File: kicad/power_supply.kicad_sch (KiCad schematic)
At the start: 60 parts, among them J2 Cliff DC10A, Q1 2N2905A, Q2 2N2905A, Q3 2N3904, Q4 2N3904, U11 7406, U16 MC34063AP, U18 LM7805_TO220, U19 LM317SP_TO220, U20 LM317SP_TO220

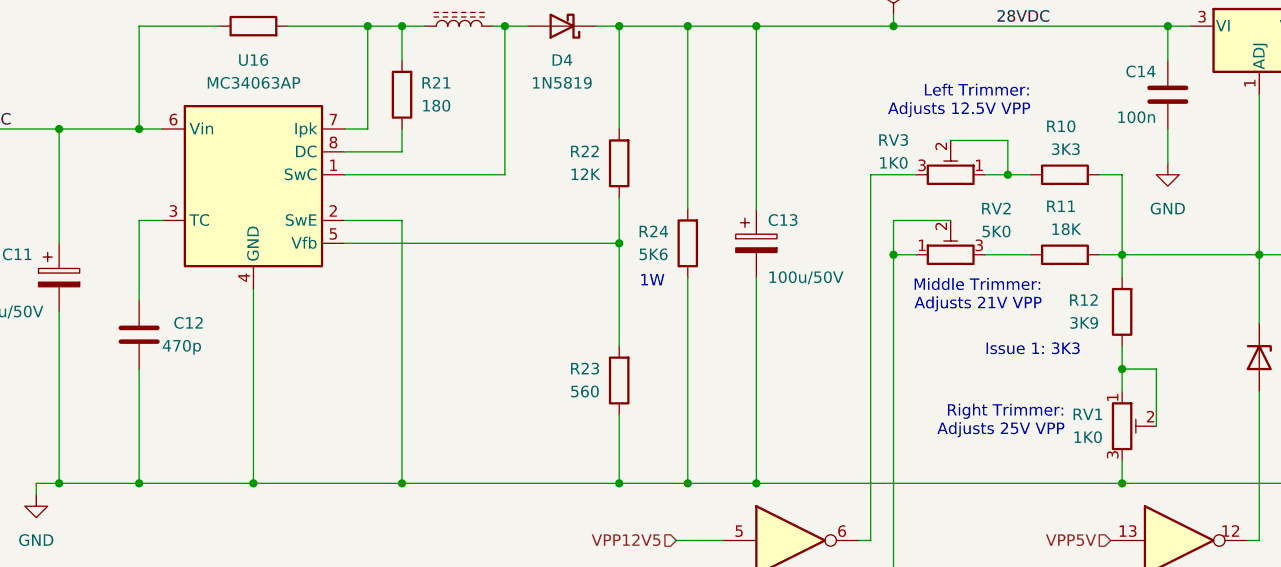
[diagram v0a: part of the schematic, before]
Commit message: KiCAD: Tweak boost convertor values
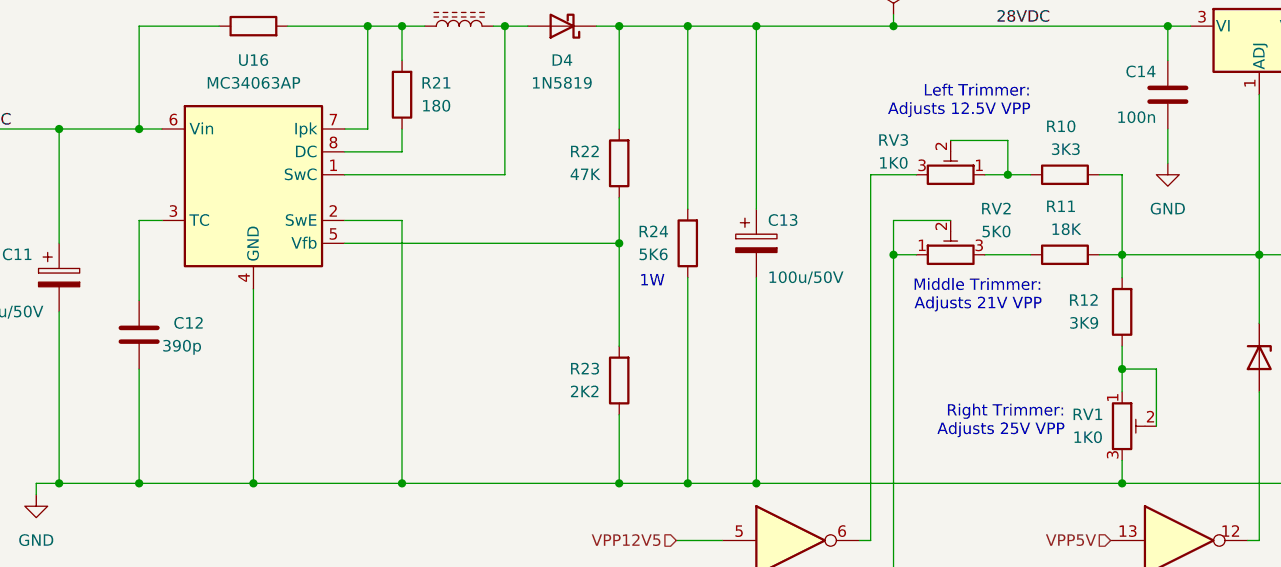
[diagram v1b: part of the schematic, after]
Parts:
- C12: value 470p -> 390p
- R22: value 12K -> 47K
- R23: value 560 -> 2K2
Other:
- note removed: "Issue 1: 3K3"
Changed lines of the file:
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@@
     (effects (font (size 1.27 1.27)) (justify right bottom))
-  )
-  (text "Issue 1: 3K3" (at 151.13 66.04 0)
-    (effects (font (size 1.27 1.27)) (justify left bottom))
   )
   (text "Indicates\nsocket is\npowered" (at 261.62 134.62 0)
@@
       (effects (font (size 1.27 1.27)) (justify right))
     )
-    (property "Value" "470p" (id 1) (at 59.69 64.77 0)
+    (property "Value" "390p" (id 1) (at 59.69 64.77 0)
       (effects (font (size 1.27 1.27)) (justify right))
     )
@@
     (in_bom yes) (on_board yes)
     (property "Reference" "R23" (id 0) (at 106.68 67.31 0))
-    (property "Value" "560" (id 1) (at 106.68 69.85 0))
+    (property "Value" "2K2" (id 1) (at 106.68 69.85 0))
     (property "Footprint" "custom_footprints:R_Axial_DIN0207_L6.3mm_D2.0mm_P10.16mm_Horizontal" (id 2) (at 112.268 68.58 90)
       (effects (font (size 1.27 1.27)) hide)
@@
     (in_bom yes) (on_board yes)
     (property "Reference" "R22" (id 0) (at 106.68 43.18 0))
-    (property "Value" "12K" (id 1) (at 106.68 45.72 0))
+    (property "Value" "47K" (id 1) (at 106.68 45.72 0))
     (property "Footprint" "custom_footprints:R_Axial_DIN0207_L6.3mm_D2.0mm_P10.16mm_Horizontal" (id 2) (at 112.268 44.45 90)
       (effects (font (size 1.27 1.27)) hide)

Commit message: KiCAD: Add heatsinks
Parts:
- added HS1: Multicomp Pro MC33263, custom_footprints:Heatsink_Fischer_SK104-STC-STIC_35x13mm_2xDrill2.5mm, symbol Mechanical:Heatsink_Pad
- added HS2, HS3: Clip On Heatsink, custom_footprints:Heatsink_Boyd_PF720, symbol Mechanical:Heatsink
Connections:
- net GND: now also HS1.1
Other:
- note removed: "Mounted on Heatsink"
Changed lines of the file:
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@@
     (effects (font (size 1.27 1.27)) (justify left bottom))
-  )
-  (text "Mounted on Heatsink" (at 68.58 124.46 180)
-    (effects (font (size 1.27 1.27)) (justify right bottom))
   )
   (text "Indicates\nboard is\npowered" (at 124.46 127 0)
@@
   (symbol (lib_id "Regulator_Linear:LM7805_TO220") (at 57.15 127 0) (unit 1)
     (in_bom yes) (on_board yes)
-    (property "Reference" "U18" (id 0) (at 57.15 118.11 0))
-    (property "Value" "LM7805_TO220" (id 1) (at 57.15 120.65 0))
+    (property "Reference" "U18" (id 0) (at 57.15 120.65 0))
+    (property "Value" "LM7805_TO220" (id 1) (at 57.15 123.19 0))
     (property "Footprint" "Package_TO_SOT_THT:TO-220-3_Vertical" (id 2) (at 57.15 121.285 0)
       (effects (font (size 1.27 1.27) italic) hide)
@@
     (pin "2")
   )
+  (symbol (lib_id "power:GND") (at 57.15 107.95 0) (unit 1)
+    (in_bom yes) (on_board yes) (fields_autoplaced)
+    (property "Reference" "#PWR0150" (id 0) (at 57.15 114.3 0)
+      (effects (font (size 1.27 1.27)) hide)
+    )
+    (property "Value" "GND" (id 1) (at 57.15 113.03 0))
+    (property "Footprint" "" (id 2) (at 57.15 107.95 0)
+      (effects (font (size 1.27 1.27)) hide)
+    )
+    (property "Datasheet" "" (id 3) (at 57.15 107.95 0)
+      (effects (font (size 1.27 1.27)) hide)
+    )
+    (pin "1")
+  )
   (symbol (lib_id "Device:C_Polarized") (at 208.28 134.62 0) (unit 1)
     (in_bom yes) (on_board yes)
@@
     (pin "3")
   )
+  (symbol (lib_id "Mechanical:Heatsink") (at 198.12 104.14 0) (unit 1)
+    (in_bom yes) (on_board yes) (fields_autoplaced)
+    (property "Reference" "HS2" (id 0) (at 201.93 100.9649 0)
+      (effects (font (size 1.27 1.27)) (justify left))
+    )
+    (property "Value" "Clip On Heatsink" (id 1) (at 201.93 103.5049 0)
+      (effects (font (size 1.27 1.27)) (justify left))
+    )
+    (property "Footprint" "custom_footprints:Heatsink_Boyd_PF720" (id 2) (at 198.4248 104.14 0)
+      (effects (font (size 1.27 1.27)) hide)
+    )
+    (property "Datasheet" "~" (id 3) (at 198.4248 104.14 0)
+      (effects (font (size 1.27 1.27)) hide)
+    )
+  )
   (symbol (lib_id "Device:LED") (at 254 134.62 90) (unit 1)
     (in_bom yes) (on_board yes) (fields_autoplaced)
@@
     (pin "2")
   )
+  (symbol (lib_id "Mechanical:Heatsink") (at 181.61 19.05 0) (unit 1)
+    (in_bom yes) (on_board yes) (fields_autoplaced)
+    (property "Reference" "HS3" (id 0) (at 185.42 15.8749 0)
+      (effects (font (size 1.27 1.27)) (justify left))
+    )
+    (property "Value" "Clip On Heatsink" (id 1) (at 185.42 18.4149 0)
+      (effects (font (size 1.27 1.27)) (justify left))
+    )
+    (property "Footprint" "custom_footprints:Heatsink_Boyd_PF720" (id 2) (at 181.9148 19.05 0)
+      (effects (font (size 1.27 1.27)) hide)
+    )
+    (property "Datasheet" "~" (id 3) (at 181.9148 19.05 0)
+      (effects (font (size 1.27 1.27)) hide)
+    )
+  )
   (symbol (lib_id "74xx:74LS06") (at 129.54 173.99 0) (unit 7)
     (in_bom yes) (on_board yes) (fields_autoplaced)
@@
     )
   )
+  (symbol (lib_id "Mechanical:Heatsink_Pad") (at 57.15 105.41 0) (unit 1)
+    (in_bom yes) (on_board yes) (fields_autoplaced)
+    (property "Reference" "HS1" (id 0) (at 60.96 103.5049 0)
+      (effects (font (size 1.27 1.27)) (justify left))
+    )
+    (property "Value" "Multicomp Pro MC33263" (id 1) (at 60.96 106.0449 0)
+      (effects (font (size 1.27 1.27)) (justify left))
+    )
+    (property "Footprint" "custom_footprints:Heatsink_Fischer_SK104-STC-STIC_35x13mm_2xDrill2.5mm" (id 2) (at 57.4548 106.68 0)
+      (effects (font (size 1.27 1.27)) hide)
+    )
+    (property "Datasheet" "~" (id 3) (at 57.4548 106.68 0)
+      (effects (font (size 1.27 1.27)) hide)
+    )
+    (pin "1")
+  )
 )

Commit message: KiCAD: Trimmers now Bourns 3296W
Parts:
- RV1, RV2, RV3: footprint custom_footprints:Potentiometer_Bourns_3339P_Vertical_HandSoldering -> Potentiometer_THT:Potentiometer_Bourns_3296W_Vertical
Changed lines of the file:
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@@
     (property "Reference" "RV3" (id 0) (at 140.97 41.91 90))
     (property "Value" "1K0" (id 1) (at 140.97 44.45 90))
-    (property "Footprint" "custom_footprints:Potentiometer_Bourns_3339P_Vertical_HandSoldering" (id 2) (at 147.32 45.72 0)
+    (property "Footprint" "Potentiometer_THT:Potentiometer_Bourns_3296W_Vertical" (id 2) (at 147.32 45.72 0)
       (effects (font (size 1.27 1.27)) hide)
     )
@@
     (property "Reference" "RV1" (id 0) (at 162.56 72.39 0))
     (property "Value" "1K0" (id 1) (at 162.56 74.93 0))
-    (property "Footprint" "custom_footprints:Potentiometer_Bourns_3339P_Vertical_HandSoldering" (id 2) (at 166.37 73.66 0)
+    (property "Footprint" "Potentiometer_THT:Potentiometer_Bourns_3296W_Vertical" (id 2) (at 166.37 73.66 0)
       (effects (font (size 1.27 1.27)) hide)
     )
@@
     (property "Reference" "RV2" (id 0) (at 152.4 49.53 90))
     (property "Value" "5K0" (id 1) (at 152.4 52.07 90))
-    (property "Footprint" "custom_footprints:Potentiometer_Bourns_3339P_Vertical_HandSoldering" (id 2) (at 147.32 54.61 0)
-      (effects (font (size 1.27 1.27)) hide)
-    )
+    (property "Footprint" "Potentiometer_THT:Potentiometer_Bourns_3296W_Vertical" (id 2) (at 147.32 54.61 0)
+      (effects (font (size 1.27 1.27)) hide)
+    )

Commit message: KiCAD: Custom footprint for inductor with multiple pads
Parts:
- L1: footprint Inductor_THT:L_Radial_D14.2mm_P10.00mm_Neosid_SD14 -> custom_footprints:L_Radial_D14.2mm_P10.00mm_Kemet
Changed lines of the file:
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@@
       (effects (font (size 1.27 1.27)) (justify left))
     )
-    (property "Footprint" "Inductor_THT:L_Radial_D14.2mm_P10.00mm_Neosid_SD14" (id 2) (at 92.71 29.21 0)
+    (property "Footprint" "custom_footprints:L_Radial_D14.2mm_P10.00mm_Kemet" (id 2) (at 92.71 29.21 0)
       (effects (font (size 1.27 1.27)) hide)
     )

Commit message: KiCAD - silk screen
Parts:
- C11, C13: value 100u/50V -> 100u
- C15: value 4.7u/35V -> 4u7
- C2: value 220u/16V -> 220u
- C8: value 10u/35V -> 10u
- C9: value 100u/16V -> 100u
- U18: value LM7805_TO220 -> LM7805
- U19, U20: value LM317SP_TO220 -> LM317T
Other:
- note added: "16V"
- note added: "35V"
- note added: "50V"
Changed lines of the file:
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@@
     (effects (font (size 1.27 1.27)) (justify right bottom))
   )
+  (text "16V" (at 220.98 140.97 0)
+    (effects (font (size 1.27 1.27)) (justify left bottom))
+  )
+  (text "50V" (at 41.91 63.5 0)
+    (effects (font (size 1.27 1.27)) (justify left bottom))
+  )
+  (text "16V" (at 60.96 138.43 0)
+    (effects (font (size 1.27 1.27)) (justify left bottom))
+  )
   (text "Indicates\nsocket is\npowered" (at 261.62 134.62 0)
+    (effects (font (size 1.27 1.27)) (justify left bottom))
+  )
+  (text "35V" (at 209.55 140.97 0)
     (effects (font (size 1.27 1.27)) (justify left bottom))
   )
@@
   )
   (text "Issue 1:\nQ3/4 are BC148" (at 238.76 46.99 0)
+    (effects (font (size 1.27 1.27)) (justify left bottom))
+  )
+  (text "50V" (at 127 59.69 0)
+    (effects (font (size 1.27 1.27)) (justify left bottom))
+  )
+  (text "35V" (at 193.04 73.66 0)
     (effects (font (size 1.27 1.27)) (justify left bottom))
   )
@@
     (in_bom yes) (on_board yes)
     (property "Reference" "U18" (id 0) (at 57.15 120.65 0))
-    (property "Value" "LM7805_TO220" (id 1) (at 57.15 123.19 0))
+    (property "Value" "LM7805" (id 1) (at 57.15 123.19 0))
     (property "Footprint" "Package_TO_SOT_THT:TO-220-3_Vertical" (id 2) (at 57.15 121.285 0)
       (effects (font (size 1.27 1.27) italic) hide)
@@
     (in_bom yes) (on_board yes)
     (property "Reference" "U19" (id 0) (at 198.12 106.68 0))
-    (property "Value" "LM317SP_TO220" (id 1) (at 198.12 109.22 0))
+    (property "Value" "LM317T" (id 1) (at 198.12 109.22 0))
     (property "Footprint" "Package_TO_SOT_THT:TO-220-3_Vertical" (id 2) (at 198.12 107.95 0)
       (effects (font (size 1.27 1.27) italic) hide)
@@
       (effects (font (size 1.27 1.27)) (justify left))
     )
-    (property "Value" "220u/16V" (id 1) (at 58.42 138.43 0)
+    (property "Value" "220u" (id 1) (at 60.96 134.62 0)
       (effects (font (size 1.27 1.27)) (justify left))
     )
@@
       (effects (font (size 1.27 1.27)) (justify left))
     )
-    (property "Value" "100u/50V" (id 1) (at 127 57.15 0)
+    (property "Value" "100u" (id 1) (at 127 55.88 0)
       (effects (font (size 1.27 1.27)) (justify left))
     )
@@
       (effects (font (size 1.27 1.27)) (justify left))
     )
-    (property "Value" "10u/35V" (id 1) (at 209.55 138.43 0)
+    (property "Value" "10u" (id 1) (at 209.55 137.16 0)
       (effects (font (size 1.27 1.27)) (justify left))
     )
@@
     (in_bom yes) (on_board yes)
     (property "Reference" "U20" (id 0) (at 181.61 21.59 0))
-    (property "Value" "LM317SP_TO220" (id 1) (at 181.61 24.13 0))
+    (property "Value" "LM317T" (id 1) (at 181.61 24.13 0))
     (property "Footprint" "Package_TO_SOT_THT:TO-220-3_Vertical" (id 2) (at 181.61 22.86 0)
       (effects (font (size 1.27 1.27) italic) hide)
@@
       (effects (font (size 1.27 1.27)) (justify left))
     )
-    (property "Value" "4.7u/35V" (id 1) (at 193.04 69.85 0)
+    (property "Value" "4u7" (id 1) (at 193.04 69.85 0)
       (effects (font (size 1.27 1.27)) (justify left))
     )
@@
       (effects (font (size 1.27 1.27)) (justify left))
     )
-    (property "Value" "100u/50V" (id 1) (at 38.1 60.96 0)
+    (property "Value" "100u" (id 1) (at 41.91 59.69 0)
       (effects (font (size 1.27 1.27)) (justify left))
     )
@@
       (effects (font (size 1.27 1.27)) (justify left))
     )
-    (property "Value" "100u/16V" (id 1) (at 220.98 138.43 0)
-      (effects (font (size 1.27 1.27)) (justify left))
-    )
+    (property "Value" "100u" (id 1) (at 220.98 137.16 0)
+      (effects (font (size 1.27 1.27)) (justify left))
+    )

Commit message: KiCAD - more silk screen
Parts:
- R13, R6: value 220 -> 220R
- R14, R7: value 470 -> 470R
- R16: value 100 -> 100R
- R21: value 180 -> 180R
- U11: footprint Package_DIP:DIP-14_W7.62mm -> Package_DIP:DIP-14_W7.62mm_Socket
- U16: footprint Package_DIP:DIP-8_W7.62mm -> Package_DIP:DIP-8_W7.62mm_Socket
- renumbered D10 to LED1, D7 to LED2, D6 to ZD1, D5 to ZD2, D11 to ZD3, D12 to ZD4
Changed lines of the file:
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@@
-    (stroke (width 0) (type default) (color 0 0 0 0))
-  )
-  (wire (pts (xy 44.45 127) (xy 45.72 127))
     (stroke (width 0) (type default) (color 0 0 0 0))
   )
@@
     (effects (font (size 1.27 1.27)) (justify left bottom))
   )
-  (text "Indicates\nsocket is\npowered" (at 261.62 134.62 0)
+  (text "Indicates\nsocket is\npowered" (at 261.62 132.08 0)
     (effects (font (size 1.27 1.27)) (justify left bottom))
   )
@@
     (property "Reference" "U11" (id 0) (at 129.54 93.345 0))
     (property "Value" "7406" (id 1) (at 129.54 90.805 0))
-    (property "Footprint" "Package_DIP:DIP-14_W7.62mm" (id 2) (at 129.54 86.36 0)
+    (property "Footprint" "Package_DIP:DIP-14_W7.62mm_Socket" (id 2) (at 129.54 86.36 0)
       (effects (font (size 1.27 1.27)) hide)
     )
@@
     (property "Reference" "U11" (id 0) (at 179.07 157.48 0))
     (property "Value" "7406" (id 1) (at 179.07 154.94 0))
-    (property "Footprint" "Package_DIP:DIP-14_W7.62mm" (id 2) (at 179.07 149.86 0)
+    (property "Footprint" "Package_DIP:DIP-14_W7.62mm_Socket" (id 2) (at 179.07 149.86 0)
       (effects (font (size 1.27 1.27)) hide)
     )
@@
       (effects (font (size 1.27 1.27)) (justify left))
     )
-    (property "Value" "470" (id 1) (at 231.648 36.576 90)
+    (property "Value" "470R" (id 1) (at 231.648 36.576 90)
       (effects (font (size 1.27 1.27)) (justify left))
     )
@@
       (effects (font (size 1.27 1.27)) (justify left))
     )
-    (property "Value" "220" (id 1) (at 210.82 121.9199 0)
+    (property "Value" "220R" (id 1) (at 210.82 121.9199 0)
       (effects (font (size 1.27 1.27)) (justify left))
     )
@@
   (symbol (lib_id "Device:D_Zener") (at 198.12 134.62 270) (unit 1)
     (in_bom yes) (on_board yes) (fields_autoplaced)
-    (property "Reference" "D6" (id 0) (at 200.66 133.3499 90)
+    (property "Reference" "ZD1" (id 0) (at 200.66 133.3499 90)
       (effects (font (size 1.27 1.27)) (justify left))
     )
@@
     (property "Reference" "U11" (id 0) (at 242.57 157.48 0))
     (property "Value" "7406" (id 1) (at 242.57 154.94 0))
-    (property "Footprint" "Package_DIP:DIP-14_W7.62mm" (id 2) (at 242.57 149.86 0)
+    (property "Footprint" "Package_DIP:DIP-14_W7.62mm_Socket" (id 2) (at 242.57 149.86 0)
       (effects (font (size 1.27 1.27)) hide)
     )
@@
       (effects (font (size 1.27 1.27)) (justify left))
     )
-    (property "Value" "470" (id 1) (at 227.838 124.206 90)
+    (property "Value" "470R" (id 1) (at 227.838 124.206 90)
       (effects (font (size 1.27 1.27)) (justify left))
     )
@@
   (symbol (lib_id "Device:D_Zener") (at 246.38 72.39 270) (unit 1)
     (in_bom yes) (on_board yes)
-    (property "Reference" "D12" (id 0) (at 248.92 71.1199 90)
+    (property "Reference" "ZD4" (id 0) (at 248.92 71.1199 90)
       (effects (font (size 1.27 1.27)) (justify left))
     )
@@
     (in_bom yes) (on_board yes)
     (property "Reference" "R21" (id 0) (at 90.17 35.56 0))
-    (property "Value" "180" (id 1) (at 90.17 38.1 0))
+    (property "Value" "180R" (id 1) (at 90.17 38.1 0))
     (property "Footprint" "custom_footprints:R_Axial_DIN0207_L6.3mm_D2.0mm_P10.16mm_Horizontal" (id 2) (at 88.138 36.83 90)
       (effects (font (size 1.27 1.27)) hide)
@@
       (effects (font (size 1.27 1.27)) (justify left))
     )
-    (property "Value" "220" (id 1) (at 194.31 43.1799 0)
+    (property "Value" "220R" (id 1) (at 194.31 43.1799 0)
       (effects (font (size 1.27 1.27)) (justify left))
     )
@@
     (property "Reference" "U11" (id 0) (at 172.72 93.98 0))
     (property "Value" "7406" (id 1) (at 172.72 91.44 0))
-    (property "Footprint" "Package_DIP:DIP-14_W7.62mm" (id 2) (at 172.72 86.36 0)
+    (property "Footprint" "Package_DIP:DIP-14_W7.62mm_Socket" (id 2) (at 172.72 86.36 0)
       (effects (font (size 1.27 1.27)) hide)
     )
@@
   (symbol (lib_id "Device:D_Zener") (at 187.96 134.62 270) (unit 1)
     (in_bom yes) (on_board yes) (fields_autoplaced)
-    (property "Reference" "D5" (id 0) (at 190.5 133.3499 90)
+    (property "Reference" "ZD2" (id 0) (at 190.5 133.3499 90)
       (effects (font (size 1.27 1.27)) (justify left))
     )
@@
   (symbol (lib_id "Device:LED") (at 254 134.62 90) (unit 1)
     (in_bom yes) (on_board yes) (fields_autoplaced)
-    (property "Reference" "D7" (id 0) (at 257.81 134.9374 90)
+    (property "Reference" "LED2" (id 0) (at 257.81 134.9374 90)
       (effects (font (size 1.27 1.27)) (justify right))
     )
@@
     (property "Reference" "U16" (id 0) (at 69.85 33.02 0))
     (property "Value" "MC34063AP" (id 1) (at 69.85 35.56 0))
-    (property "Footprint" "Package_DIP:DIP-8_W7.62mm" (id 2) (at 71.12 57.15 0)
+    (property "Footprint" "Package_DIP:DIP-8_W7.62mm_Socket" (id 2) (at 71.12 57.15 0)
       (effects (font (size 1.27 1.27)) (justify left) hide)
     )
@@
     (property "Reference" "U11" (id 0) (at 161.29 166.37 0))
     (property "Value" "7406" (id 1) (at 161.29 168.91 0))
-    (property "Footprint" "Package_DIP:DIP-14_W7.62mm" (id 2) (at 161.29 175.26 0)
+    (property "Footprint" "Package_DIP:DIP-14_W7.62mm_Socket" (id 2) (at 161.29 175.26 0)
       (effects (font (size 1.27 1.27)) hide)
     )
@@
   (symbol (lib_id "Device:LED") (at 119.38 138.43 90) (unit 1)
     (in_bom yes) (on_board yes)
-    (property "Reference" "D10" (id 0) (at 121.92 137.16 90)
+    (property "Reference" "LED1" (id 0) (at 121.92 137.16 90)
       (effects (font (size 1.27 1.27)) (justify right))
     )
@@
       (effects (font (size 1.27 1.27)) (justify left))
     )
-    (property "Footprint" "Package_DIP:DIP-14_W7.62mm" (id 2) (at 129.54 173.99 0)
+    (property "Footprint" "Package_DIP:DIP-14_W7.62mm_Socket" (id 2) (at 129.54 173.99 0)
       (effects (font (size 1.27 1.27)) hide)
     )
@@
   )
   (symbol (lib_id "Device:D_Zener") (at 181.61 66.04 270) (unit 1)
-    (in_bom yes) (on_board yes) (fields_autoplaced)
-    (property "Reference" "D11" (id 0) (at 184.15 64.7699 90)
+    (in_bom yes) (on_board yes)
+    (property "Reference" "ZD3" (id 0) (at 184.15 64.7699 90)
       (effects (font (size 1.27 1.27)) (justify left))
     )
@@
       (effects (font (size 1.27 1.27)) (justify left))
     )
-    (property "Value" "100" (id 1) (at 227.33 54.6099 0)
+    (property "Value" "100R" (id 1) (at 227.33 54.6099 0)
       (effects (font (size 1.27 1.27)) (justify left))
     )
@@
     (property "Reference" "U11" (id 0) (at 129.54 106.045 0))
     (property "Value" "7406" (id 1) (at 129.54 103.505 0))
-    (property "Footprint" "Package_DIP:DIP-14_W7.62mm" (id 2) (at 129.54 98.425 0)
-      (effects (font (size 1.27 1.27)) hide)
-    )
+    (property "Footprint" "Package_DIP:DIP-14_W7.62mm_Socket" (id 2) (at 129.54 98.425 0)
+      (effects (font (size 1.27 1.27)) hide)
+    )
